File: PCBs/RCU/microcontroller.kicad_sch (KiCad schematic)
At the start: 26 parts

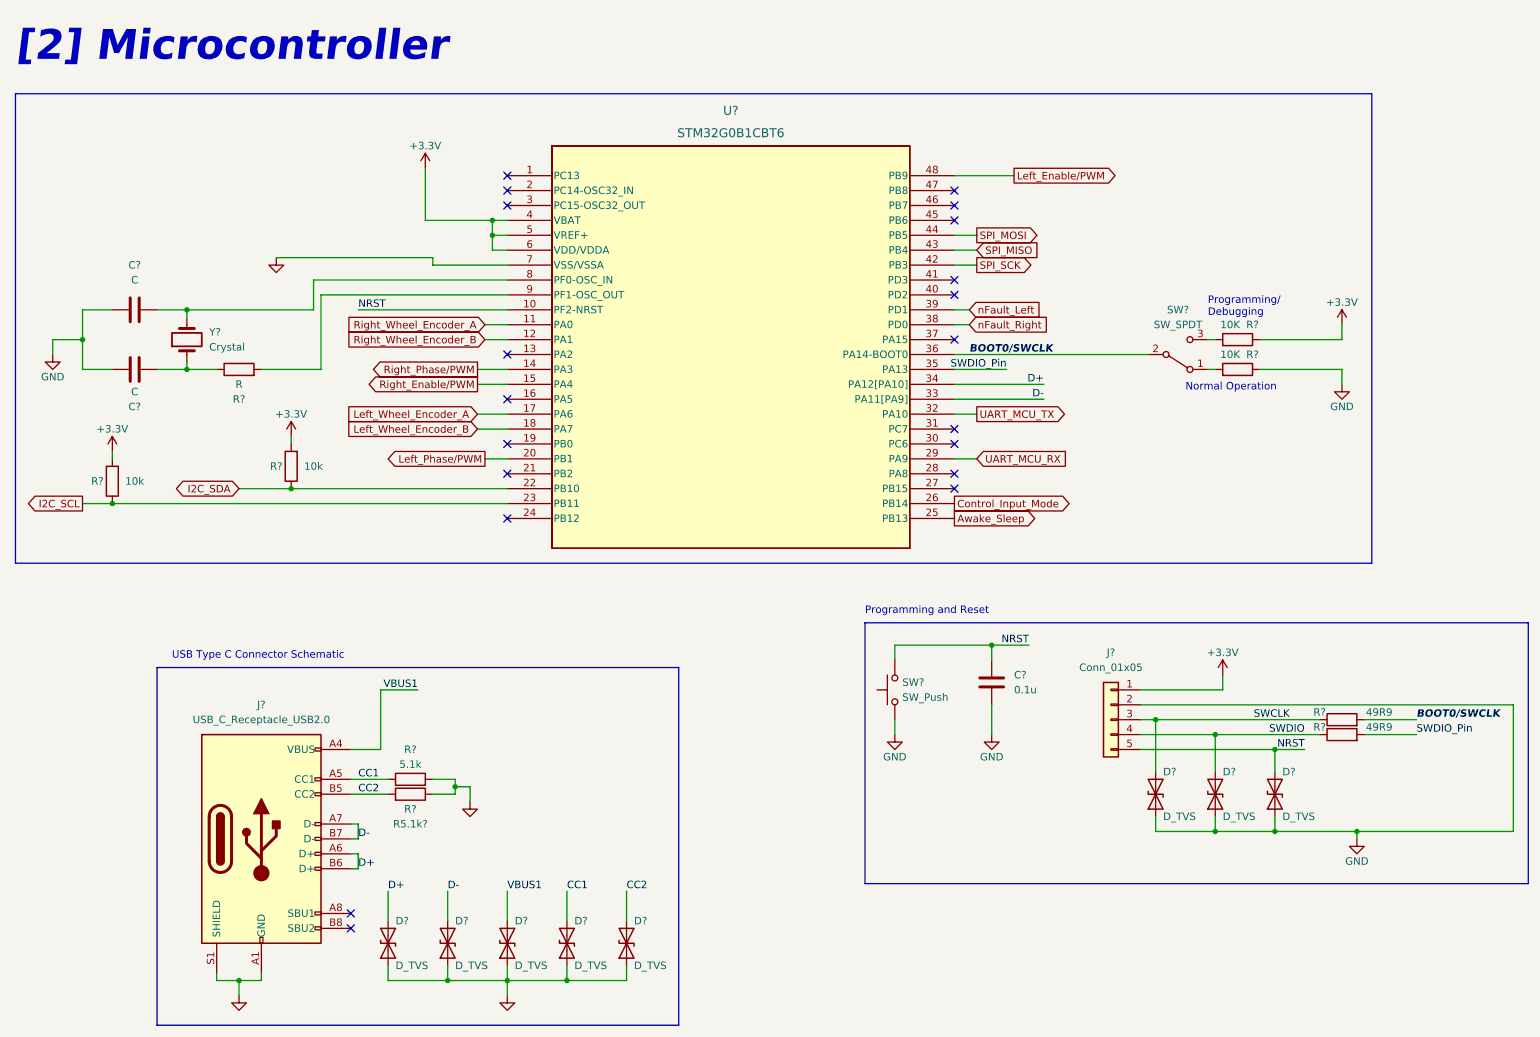
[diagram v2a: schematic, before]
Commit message: Annotated all microcontroller components
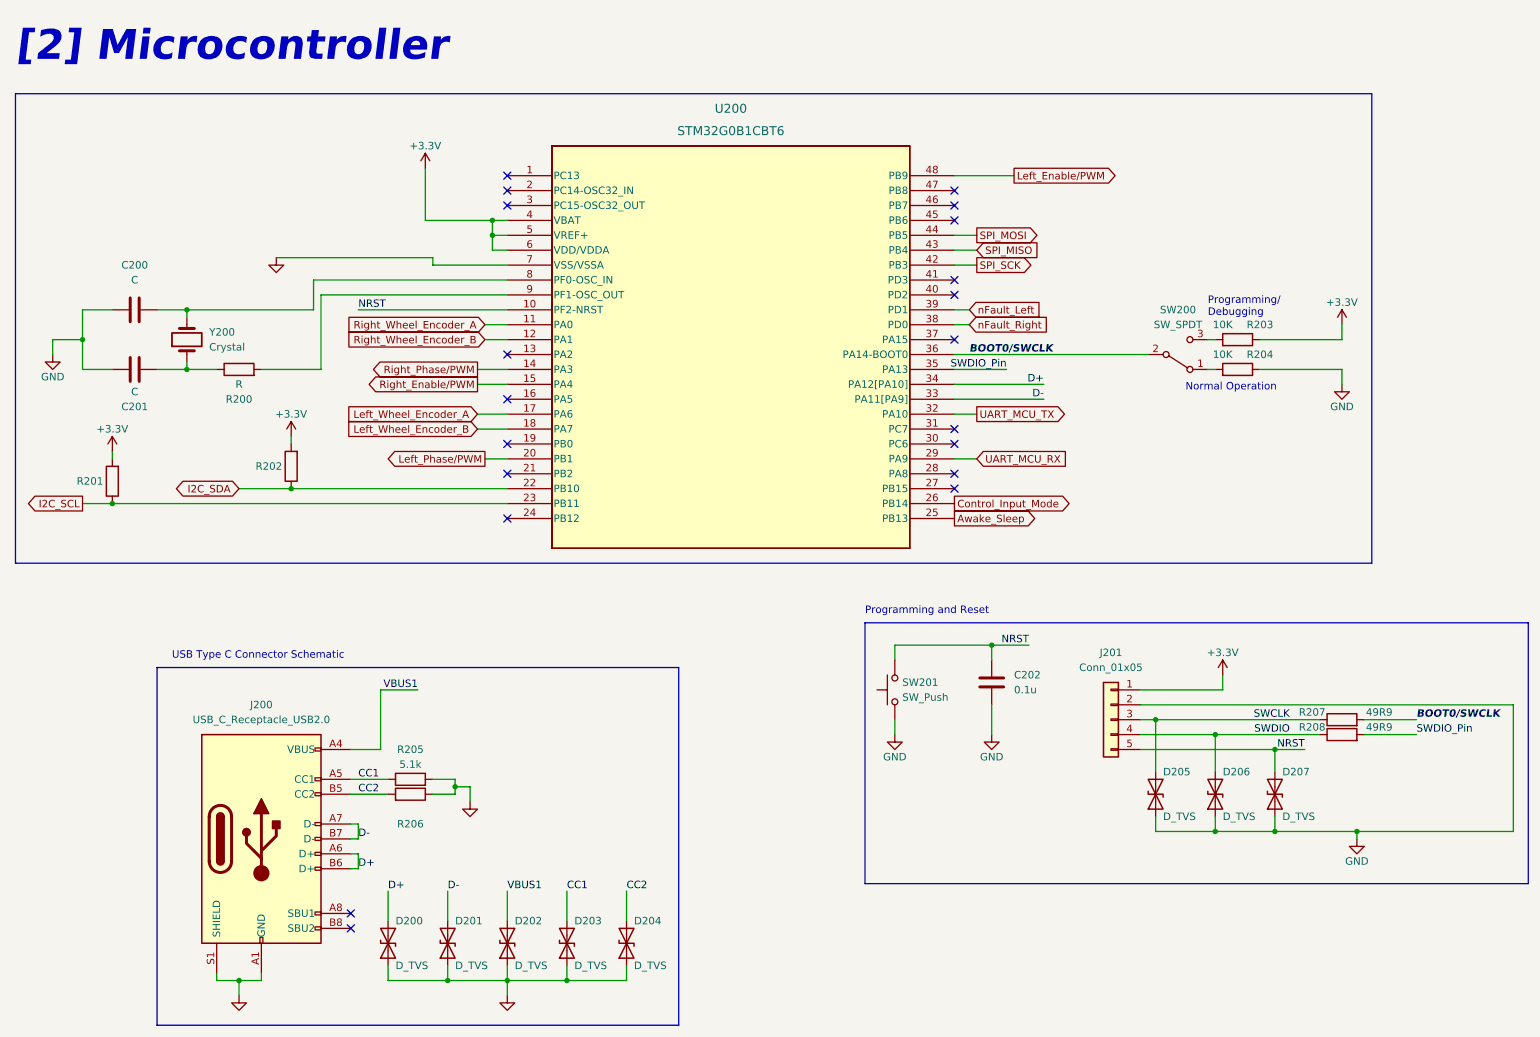
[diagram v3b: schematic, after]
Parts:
- R201, R202: renamed from R?; value 10k -> (none)
- R206: renamed from R5.1k?; value R? -> (none)
- gave numbers to parts that had none: 23
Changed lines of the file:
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@@
     (effects (font (size 1.27 1.27)) (justify left bottom))
   )
-  (label "SWDIO" (at 238.76 138.43 180)
+  (label "SWDIO" (at 236.22 138.43 180)
     (effects (font (size 1.27 1.27)) (justify right bottom))
   )
@@
   (symbol (lib_id "Connector_Generic:Conn_01x05") (at 205.74 135.89 0) (mirror y) (unit 1)
     (in_bom yes) (on_board yes) (fields_autoplaced)
-    (property "Reference" "J?" (id 0) (at 205.74 124.46 0))
+    (property "Reference" "J201" (id 0) (at 205.74 124.46 0))
     (property "Value" "Conn_01x05" (id 1) (at 205.74 127 0))
     (property "Footprint" "" (id 2) (at 205.74 135.89 0)
@@
   (symbol (lib_id "Device:R") (at 66.04 92.71 180) (unit 1)
     (in_bom yes) (on_board yes)
-    (property "Reference" "R?" (id 0) (at 63.5 92.71 0))
-    (property "Value" "10k" (id 1) (at 69.85 92.71 0))
+    (property "Reference" "R202" (id 0) (at 62.23 92.71 0))
+    (property "Value" "" (id 1) (at 69.85 92.71 0))
     (property "Footprint" "" (id 2) (at 67.818 92.71 90)
       (effects (font (size 1.27 1.27)) hide)
@@
   (symbol (lib_id "Device:R") (at 86.36 148.59 270) (mirror x) (unit 1)
     (in_bom yes) (on_board yes)
-    (property "Reference" "R5.1k?" (id 0) (at 86.36 153.67 90))
-    (property "Value" "R?" (id 1) (at 86.36 151.13 90))
+    (property "Reference" "R206" (id 0) (at 86.36 153.67 90))
+    (property "Value" "" (id 1) (at 86.36 151.13 90))
     (property "Footprint" "" (id 2) (at 86.36 150.368 90)
       (effects (font (size 1.27 1.27)) hide)
@@
   (symbol (lib_id "Device:R") (at 245.11 138.43 90) (unit 1)
     (in_bom yes) (on_board yes)
-    (property "Reference" "R?" (id 0) (at 241.3 137.16 90))
+    (property "Reference" "R208" (id 0) (at 240.03 137.16 90))
     (property "Value" "49R9" (id 1) (at 251.46 137.16 90))
     (property "Footprint" "" (id 2) (at 245.11 140.208 90)
@@
   (symbol (lib_id "Device:C") (at 39.37 76.2 90) (unit 1)
     (in_bom yes) (on_board yes)
-    (property "Reference" "C?" (id 0) (at 39.37 82.55 90))
+    (property "Reference" "C201" (id 0) (at 39.37 82.55 90))
     (property "Value" "C" (id 1) (at 39.37 80.01 90))
     (property "Footprint" "" (id 2) (at 43.18 75.2348 0)
@@
   (symbol (lib_id "Switch:SW_Push") (at 168.91 130.81 90) (unit 1)
     (in_bom yes) (on_board yes) (fields_autoplaced)
-    (property "Reference" "SW?" (id 0) (at 170.18 129.5399 90)
+    (property "Reference" "SW201" (id 0) (at 170.18 129.5399 90)
       (effects (font (size 1.27 1.27)) (justify right))
     )
@@
   (symbol (lib_id "Device:R") (at 35.56 95.25 180) (unit 1)
     (in_bom yes) (on_board yes)
-    (property "Reference" "R?" (id 0) (at 33.02 95.25 0))
-    (property "Value" "10k" (id 1) (at 39.37 95.25 0))
+    (property "Reference" "R201" (id 0) (at 31.75 95.25 0))
+    (property "Value" "" (id 1) (at 39.37 95.25 0))
     (property "Footprint" "" (id 2) (at 37.338 95.25 90)
       (effects (font (size 1.27 1.27)) hide)
@@
   (symbol (lib_id "Device:R") (at 227.33 76.2 270) (mirror x) (unit 1)
     (in_bom yes) (on_board yes)
-    (property "Reference" "R?" (id 0) (at 229.87 73.66 90))
-    (property "Value" "10K" (id 1) (at 226.06 73.66 90))
+    (property "Reference" "R204" (id 0) (at 231.14 73.66 90))
+    (property "Value" "10K" (id 1) (at 224.79 73.66 90))
     (property "Footprint" "" (id 2) (at 227.33 77.978 90)
       (effects (font (size 1.27 1.27)) hide)
@@
   (symbol (lib_id "Device:D_TVS") (at 233.68 148.59 90) (unit 1)
     (in_bom yes) (on_board yes)
-    (property "Reference" "D?" (id 0) (at 234.95 144.78 90)
+    (property "Reference" "D207" (id 0) (at 234.95 144.78 90)
       (effects (font (size 1.27 1.27)) (justify right))
     )
@@
   (symbol (lib_id "Device:D_TVS") (at 213.36 148.59 90) (unit 1)
     (in_bom yes) (on_board yes)
-    (property "Reference" "D?" (id 0) (at 214.63 144.78 90)
+    (property "Reference" "D205" (id 0) (at 214.63 144.78 90)
       (effects (font (size 1.27 1.27)) (justify right))
     )
@@
   (symbol (lib_id "Device:Crystal") (at 48.26 71.12 90) (unit 1)
     (in_bom yes) (on_board yes) (fields_autoplaced)
-    (property "Reference" "Y?" (id 0) (at 52.07 69.8499 90)
+    (property "Reference" "Y200" (id 0) (at 52.07 69.8499 90)
       (effects (font (size 1.27 1.27)) (justify right))
     )
@@
   (symbol (lib_id "Switch:SW_SPDT") (at 217.17 73.66 0) (mirror x) (unit 1)
     (in_bom yes) (on_board yes) (fields_autoplaced)
-    (property "Reference" "SW?" (id 0) (at 217.17 66.04 0))
+    (property "Reference" "SW200" (id 0) (at 217.17 66.04 0))
     (property "Value" "SW_SPDT" (id 1) (at 217.17 68.58 0))
     (property "Footprint" "" (id 2) (at 217.17 73.66 0)
@@
   (symbol (lib_id "Device:R") (at 227.33 71.12 270) (mirror x) (unit 1)
     (in_bom yes) (on_board yes)
-    (property "Reference" "R?" (id 0) (at 229.87 68.58 90))
-    (property "Value" "10K" (id 1) (at 226.06 68.58 90))
+    (property "Reference" "R203" (id 0) (at 231.14 68.58 90))
+    (property "Value" "10K" (id 1) (at 224.79 68.58 90))
     (property "Footprint" "" (id 2) (at 227.33 72.898 90)
       (effects (font (size 1.27 1.27)) hide)
@@
   (symbol (lib_id "Device:C") (at 39.37 66.04 270) (unit 1)
     (in_bom yes) (on_board yes) (fields_autoplaced)
-    (property "Reference" "C?" (id 0) (at 39.37 58.42 90))
+    (property "Reference" "C200" (id 0) (at 39.37 58.42 90))
     (property "Value" "C" (id 1) (at 39.37 60.96 90))
     (property "Footprint" "" (id 2) (at 35.56 67.0052 0)
@@
   (symbol (lib_id "Device:D_TVS") (at 223.52 148.59 90) (unit 1)
     (in_bom yes) (on_board yes)
-    (property "Reference" "D?" (id 0) (at 224.79 144.78 90)
+    (property "Reference" "D206" (id 0) (at 224.79 144.78 90)
       (effects (font (size 1.27 1.27)) (justify right))
     )
@@
   (symbol (lib_id "Device:D_TVS") (at 113.03 173.99 90) (unit 1)
     (in_bom yes) (on_board yes)
-    (property "Reference" "D?" (id 0) (at 114.3 170.18 90)
+    (property "Reference" "D203" (id 0) (at 114.3 170.18 90)
       (effects (font (size 1.27 1.27)) (justify right))
     )
@@
   (symbol (lib_id "Device:D_TVS") (at 82.55 173.99 90) (unit 1)
     (in_bom yes) (on_board yes)
-    (property "Reference" "D?" (id 0) (at 83.82 170.18 90)
+    (property "Reference" "D200" (id 0) (at 83.82 170.18 90)
       (effects (font (size 1.27 1.27)) (justify right))
     )
@@
   (symbol (lib_id "2024-04-19_01-31-40:STM32G0B1CBT6") (at 102.87 43.18 0) (unit 1)
     (in_bom yes) (on_board yes) (fields_autoplaced)
-    (property "Reference" "U?" (id 0) (at 140.97 32.1056 0)
+    (property "Reference" "U200" (id 0) (at 140.97 31.75 0)
       (effects (font (size 1.524 1.524)))
     )
-    (property "Value" "STM32G0B1CBT6" (id 1) (at 140.97 35.9156 0)
+    (property "Value" "STM32G0B1CBT6" (id 1) (at 140.97 35.56 0)
       (effects (font (size 1.524 1.524)))
     )
@@
   (symbol (lib_id "Device:D_TVS") (at 92.71 173.99 90) (unit 1)
     (in_bom yes) (on_board yes)
-    (property "Reference" "D?" (id 0) (at 93.98 170.18 90)
+    (property "Reference" "D201" (id 0) (at 93.98 170.18 90)
       (effects (font (size 1.27 1.27)) (justify right))
     )
@@
   (symbol (lib_id "Device:R") (at 86.36 146.05 90) (unit 1)
     (in_bom yes) (on_board yes)
-    (property "Reference" "R?" (id 0) (at 86.36 140.97 90))
+    (property "Reference" "R205" (id 0) (at 86.36 140.97 90))
     (property "Value" "5.1k" (id 1) (at 86.36 143.51 90))
     (property "Footprint" "" (id 2) (at 86.36 147.828 90)
@@
   (symbol (lib_id "Device:R") (at 245.11 135.89 90) (unit 1)
     (in_bom yes) (on_board yes)
-    (property "Reference" "R?" (id 0) (at 241.3 134.62 90))
+    (property "Reference" "R207" (id 0) (at 240.03 134.62 90))
     (property "Value" "49R9" (id 1) (at 251.46 134.62 90))
     (property "Footprint" "" (id 2) (at 245.11 137.668 90)
@@
   (symbol (lib_id "Connector:USB_C_Receptacle_USB2.0") (at 60.96 156.21 0) (unit 1)
     (in_bom yes) (on_board yes) (fields_autoplaced)
-    (property "Reference" "J?" (id 0) (at 60.96 133.35 0))
+    (property "Reference" "J200" (id 0) (at 60.96 133.35 0))
     (property "Value" "USB_C_Receptacle_USB2.0" (id 1) (at 60.96 135.89 0))
     (property "Footprint" "" (id 2) (at 64.77 156.21 0)
@@
   (symbol (lib_id "Device:D_TVS") (at 123.19 173.99 90) (unit 1)
     (in_bom yes) (on_board yes)
-    (property "Reference" "D?" (id 0) (at 124.46 170.18 90)
+    (property "Reference" "D204" (id 0) (at 124.46 170.18 90)
       (effects (font (size 1.27 1.27)) (justify right))
     )
@@
   (symbol (lib_id "Device:D_TVS") (at 102.87 173.99 90) (unit 1)
     (in_bom yes) (on_board yes)
-    (property "Reference" "D?" (id 0) (at 104.14 170.18 90)
+    (property "Reference" "D202" (id 0) (at 104.14 170.18 90)
       (effects (font (size 1.27 1.27)) (justify right))
     )
@@
   (symbol (lib_id "Device:C") (at 185.42 129.54 0) (unit 1)
     (in_bom yes) (on_board yes) (fields_autoplaced)
-    (property "Reference" "C?" (id 0) (at 189.23 128.2699 0)
+    (property "Reference" "C202" (id 0) (at 189.23 128.2699 0)
       (effects (font (size 1.27 1.27)) (justify left))
     )
@@
   (symbol (lib_id "Device:R") (at 57.15 76.2 90) (unit 1)
     (in_bom yes) (on_board yes)
-    (property "Reference" "R?" (id 0) (at 57.15 81.28 90))
+    (property "Reference" "R200" (id 0) (at 57.15 81.28 90))
     (property "Value" "R" (id 1) (at 57.15 78.74 90))
     (property "Footprint" "" (id 2) (at 57.15 77.978 90)

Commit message: Finished labelling all of microcontroller schematic
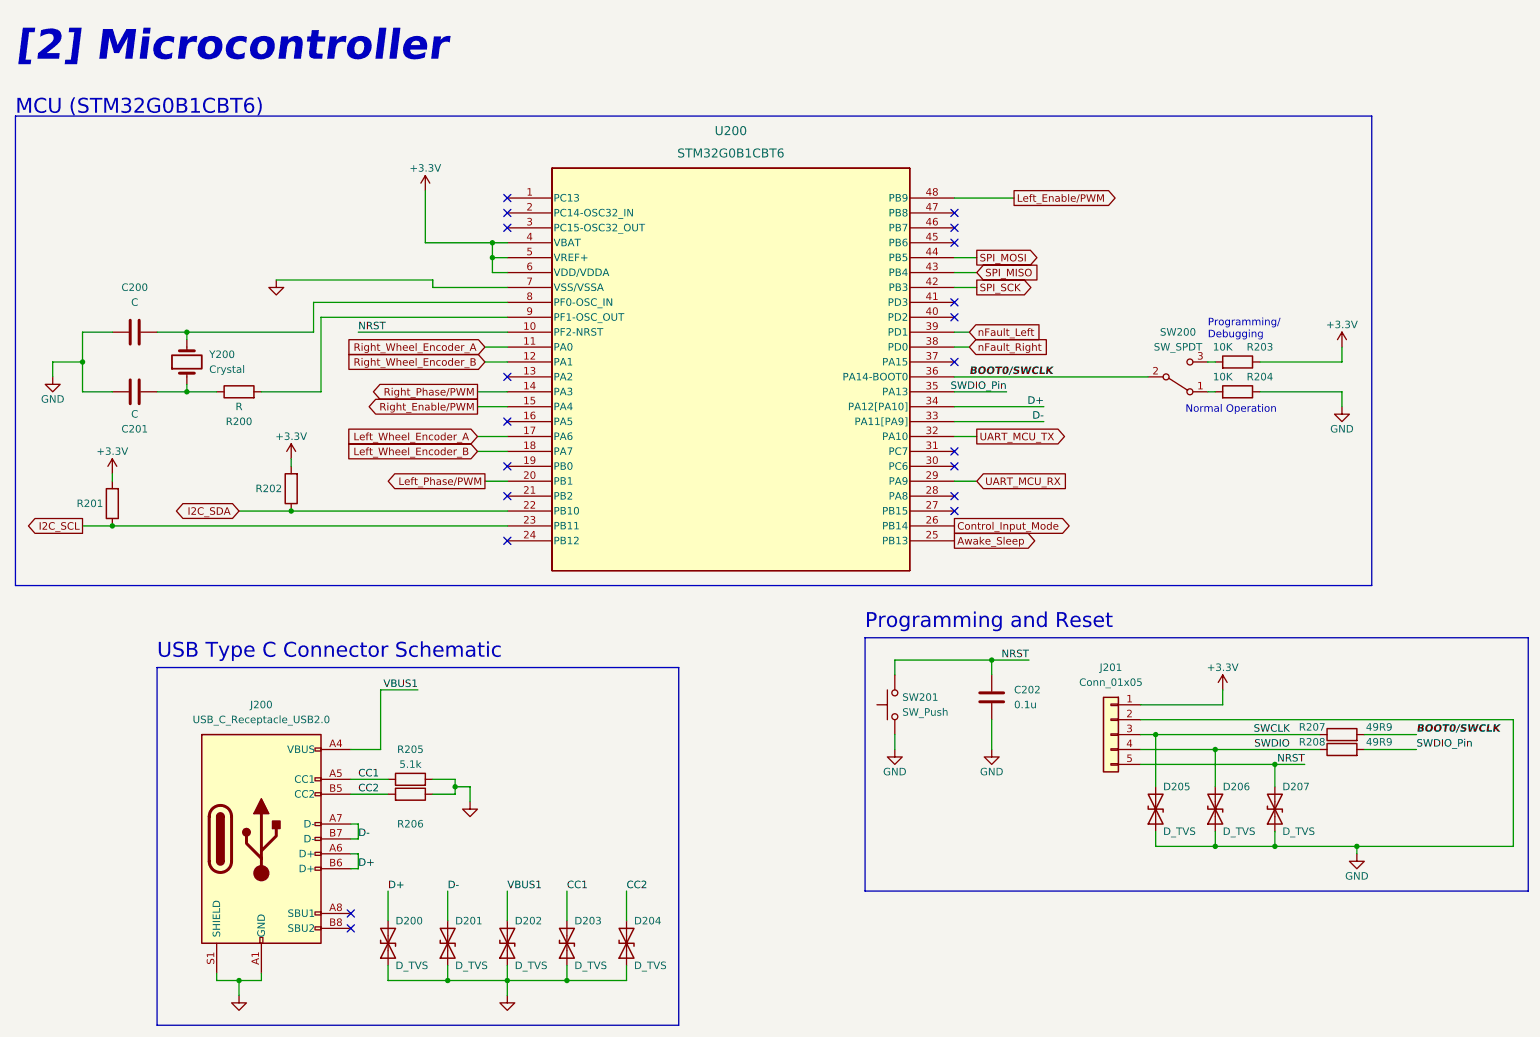
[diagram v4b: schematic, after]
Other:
- note added: "MCU (STM32G0B1CBT6)"
- moved on the sheet: C200, C201, C202, D205, D206, D207, J201, R200, R201, R202, R203, R204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
